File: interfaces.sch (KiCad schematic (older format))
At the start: 55 parts, among them J6 0878311420, J7 61300611121, U14 XC7A100T-FGG484, U17 EMMC04G-S100-B08U, U18 MAX3421EEHJ, U19 FT245RQ, U6 NVT2008DQ,115, Y1 ABM8G-12.000MHZ-18-D2Y-T

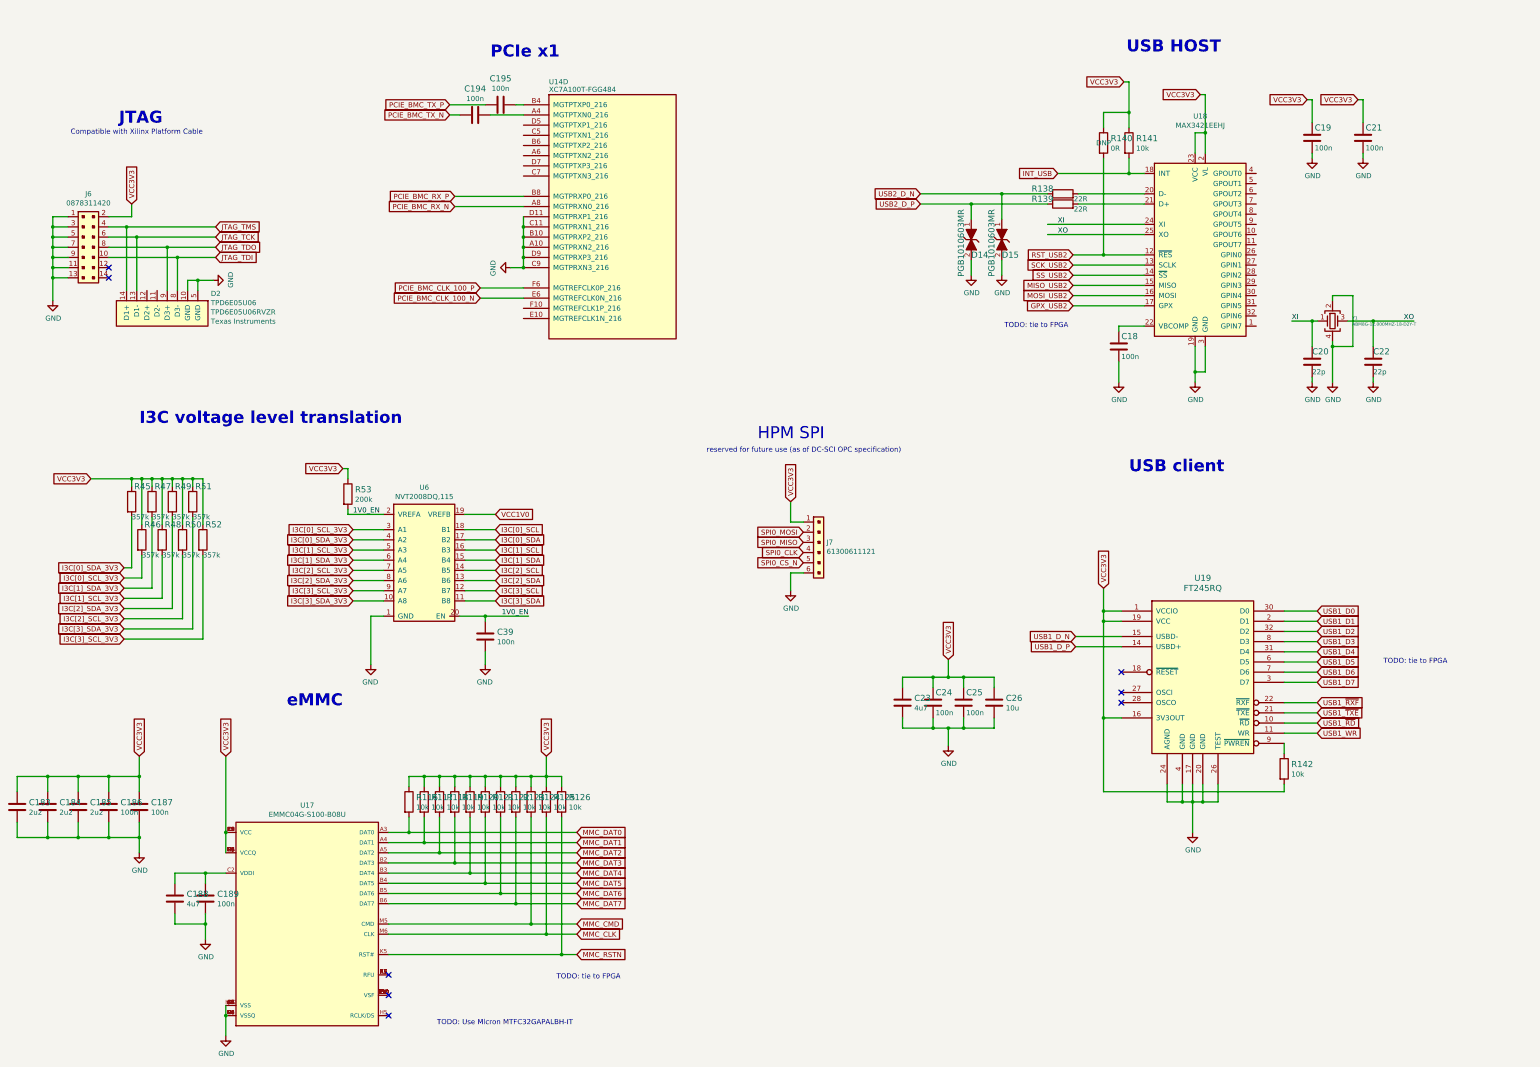
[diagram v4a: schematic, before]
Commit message: Added USB3300 controllers
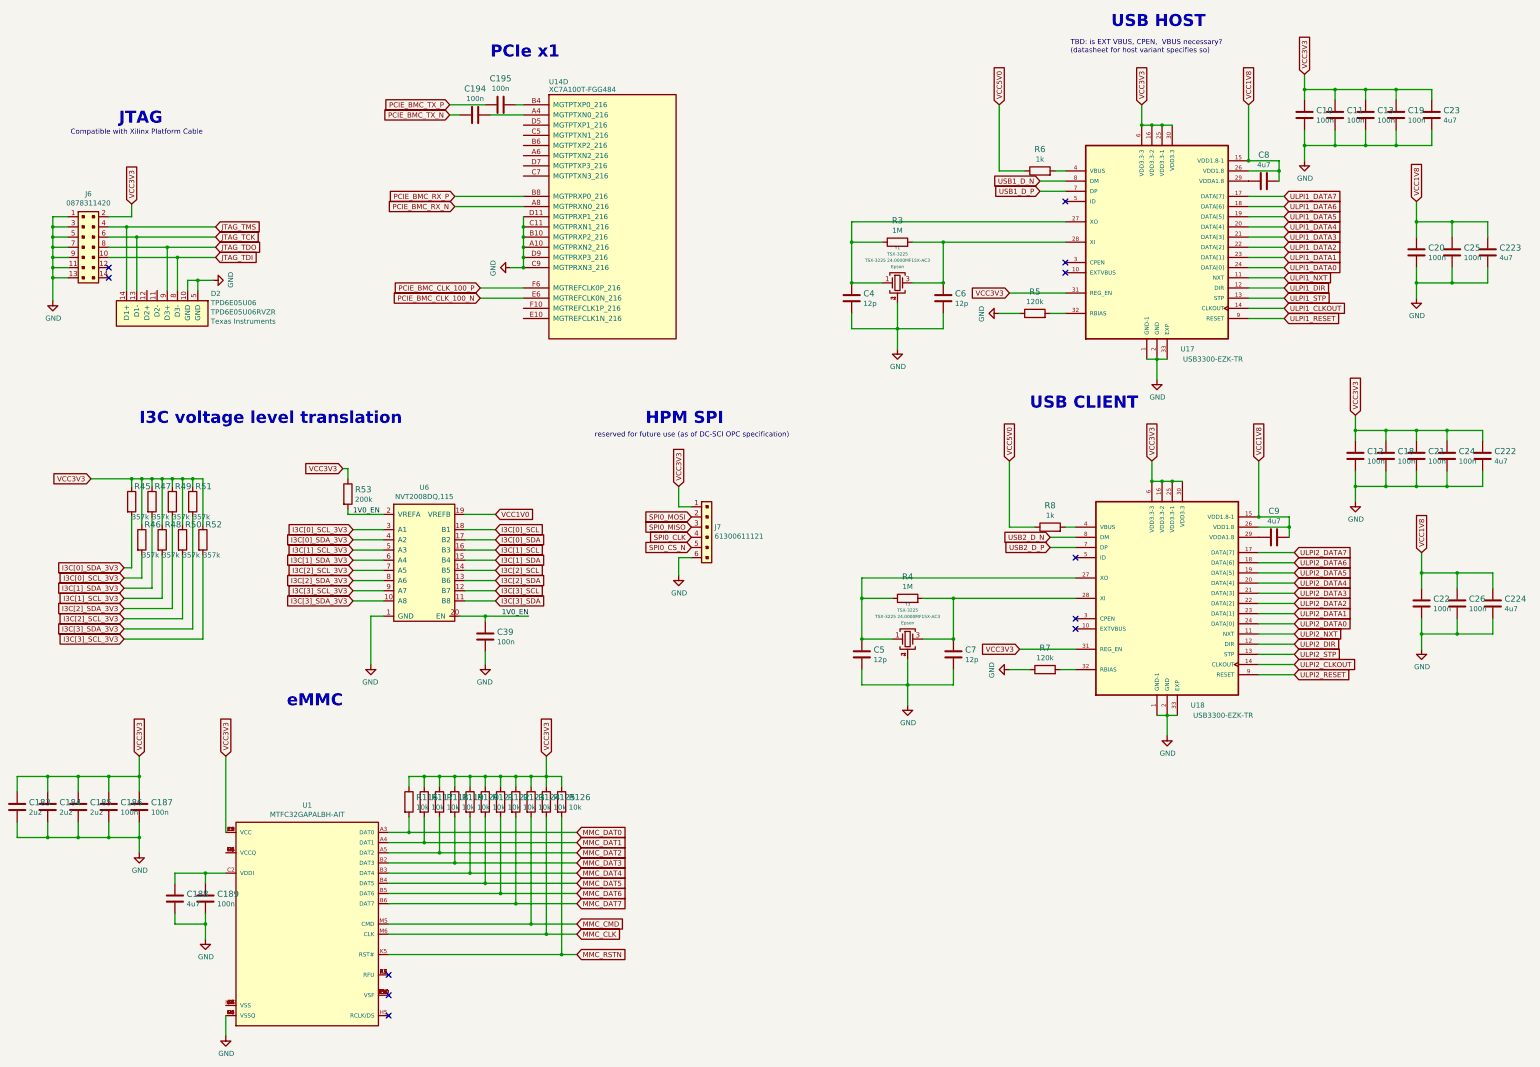
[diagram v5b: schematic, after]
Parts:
- removed C18, C19, C21, C24, C25: C_100n_0402, artix-dc-scm-footprints:0402-cap, symbol artix-dc-scm:C_100n_0402-artix-dc-scm
- removed C20, C22: C_22p_0402, artix-dc-scm-footprints:0402-cap, symbol artix-dc-scm:C_22p_0402
- removed C23: C_4u7_0402, artix-dc-scm-footprints:0402-cap, symbol artix-dc-scm:C_4u7_0402
- removed C26: C_10u_0402, artix-dc-scm-footprints:0402-cap, symbol artix-dc-scm:C_10u_0402
- removed D14, D15: PGB1010603MR, artix-dc-scm-footprints:PGB1010603MR, symbol artix-dc-scm:PGB1010603MR
- removed R138, R139: R_22R_0402, artix-dc-scm-footprints:0402-res, symbol artix-dc-scm:R_22R_0402
- removed R140: R_0R_0402, artix-dc-scm-footprints:0402-res, symbol artix-dc-scm:R_0R_0402
- removed R141, R142: R_10k_0402, artix-dc-scm-footprints:0402-res, symbol artix-dc-scm:R_10k_0402
- removed U17: EMMC04G-S100-B08U, artix-dc-scm-footprints:MICRON_EMMC_153, symbol artix-dc-scm:EMMC04G-S100-B08U
- removed U18: MAX3421EEHJ, artix-dc-scm-footprints:TQFP-32_5x5mm, symbol artix-dc-scm:MAX3421EEHJ
- removed U19: FT245RQ, artix-dc-scm-footprints:QFN-32-1EP_5x5mm, symbol artix-dc-scm:FT245RQ
- removed Y1: ABM8G-12.000MHZ-18-D2Y-T, artix-dc-scm-footprints:KX-7, symbol artix-dc-scm:ABM8G-12.000MHZ-18-D2Y-T
- added C10, C11, C12, C13, C18, C19, C20, C21, C22, C24, C25, C26: C_100n_0402, antmicro-footprints:0402-cap, symbol antmicroCapacitors0402:C_100n_0402
- added C222, C223, C224, C23, C8, C9: C_4u7_0402, antmicro-footprints:0402-cap, symbol antmicroCapacitors0402:C_4u7_0402
- added C4, C5, C6, C7: C_12p_0402, antmicro-footprints:0402-cap, symbol antmicroCapacitors0402:C_12p_0402
- added R3, R4: R_1M_0603, antmicro-footprints:0603-res, symbol antmicroResistors0603:R_1M_0603
- added R5, R7: R_120k_0402, antmicro-footprints:0402-res, symbol antmicroResistors0402:R_120k_0402
- added R6, R8: R_1k_0402, antmicro-footprints:0402-res, symbol antmicroResistors0402:R_1k_0402
- added U1: MTFC32GAPALBH-AIT, antmicro-footprints:MICRON_EMMC_153, symbol antmicroMemory:MTFC32GAPALBH-AIT
- added U17, U18: USB3300-EZK-TR, QFN50P500X500X100-33N, symbol antmicroInterfaceControllers:USB3300-EZK-TR
- added Y1, Y3: TSX-3225, antmicro-footprints:KX-7, symbol antmicroCrystals:TSX-3225
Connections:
- net GND: now also C10.2, C11.2, C12.2, C13.2, C18.2, C19.2, C20.2, C21.2, C22.2, C222.2, C223.2, C224.2, C23.2, C24.2, C25.2, C26.2, C4.2, C5.2, C6.2, C7.2, R5.1, R7.1, U1.C4 (VSSQ), U1.N2 (VSSQ), U1.N5 (VSSQ), U1.P4 (VSSQ), U1.P6 (VSSQ), U17.1 (GND-1), U17.2 (GND), U17.33 (EXP), U18.1 (GND-1), U18.2 (GND), U18.33 (EXP), Y1.2, Y1.4, Y3.2, Y3.4
- net MMC_CLK: now also U1.M6 (CLK)
- net MMC_CMD: now also U1.M5 (CMD)
- net MMC_DAT0: now also U1.A3 (DAT0)
- net MMC_DAT1: now also U1.A4 (DAT1)
- net MMC_DAT2: now also U1.A5 (DAT2)
- net MMC_DAT3: now also U1.B2 (DAT3)
- net MMC_DAT4: now also U1.B3 (DAT4)
- net MMC_DAT5: now also U1.B4 (DAT5)
- net MMC_DAT6: now also U1.B5 (DAT6)
- net MMC_DAT7: now also U1.B6 (DAT7)
- net MMC_RSTN: now also U1.K5 (RST#)
- net USB1_D_N: now also U17.8 (DM)
- net USB1_D_P: now also U17.7 (DP)
- net USB2_D_N: now also U18.8 (DM)
- net USB2_D_P: now also U18.7 (DP)
- net VCC3V3: now also C10.1, C11.1, C12.1, C13.1, C18.1, C19.1, C21.1, C222.1, C23.1, C24.1, U1.E6 (VCC), U1.F5 (VCC), U1.J10 (VCC), U1.K9 (VCC), U17.16 (VDD3.3-2), U17.25 (VDD3.3-1), U17.30 (VDD3.3), U17.31 (REG_EN), U17.6 (VDD3.3-3), U18.16 (VDD3.3-2), U18.25 (VDD3.3-1), U18.30 (VDD3.3), U18.31 (REG_EN), U18.6 (VDD3.3-3)
- net at C188.1, C189.1: now also U1.C2 (VDDI)
- new net: C4.1, R3.1, U17.27 (XO), Y1.1
- new net: C6.1, R3.2, U17.28 (XI), Y1.3
- new net: C8.2, U17.29 (VDDA1.8)
- new net: R5.2, U17.32 (RBIAS)
- new net: R6.2, U17.4 (VBUS)
- new net: C5.1, R4.1, U18.27 (XO), Y3.1
- new net: C7.1, R4.2, U18.28 (XI), Y3.3
- new net: C9.2, U18.29 (VDDA1.8)
- new net: R7.2, U18.32 (RBIAS)
- new net: R8.2, U18.4 (VBUS)
- new net: U1.A6 (VSS), U1.E7 (VSS), U1.G5 (VSS), U1.H10 (VSS), U1.J5 (VSS), U1.K8 (VSS)
- new net: U1.A7 (RFU), U1.E5 (RFU), U1.K6 (RFU), U1.K7 (RFU)
- new net: U1.C6 (VCCQ), U1.M4 (VCCQ), U1.N4 (VCCQ), U1.P3 (VCCQ), U1.P5 (VCCQ)
- new net: U1.E10 (VSF), U1.E8 (VSF), U1.E9 (VSF), U1.F10 (VSF), U1.G10 (VSF), U1.K10 (VSF), U1.P10 (VSF)
- new net ULPI1_CLKOUT: U17.14 (CLKOUT)
- new net ULPI1_DATA0: U17.24 (DATA[0])
- new net ULPI1_DATA1: U17.23 (DATA[1])
- new net ULPI1_DATA2: U17.22 (DATA[2])
- new net ULPI1_DATA3: U17.21 (DATA[3])
- new net ULPI1_DATA4: U17.20 (DATA[4])
- new net ULPI1_DATA5: U17.19 (DATA[5])
- new net ULPI1_DATA6: U17.18 (DATA[6])
- new net ULPI1_DATA7: U17.17 (DATA[7])
- new net ULPI1_DIR: U17.12 (DIR)
- new net ULPI1_NXT: U17.11 (NXT)
- new net ULPI1_RESET: U17.9 (RESET)
- new net ULPI1_STP: U17.13 (STP)
- new net ULPI2_CLKOUT: U18.14 (CLKOUT)
- new net ULPI2_DATA0: U18.24 (DATA[0])
- new net ULPI2_DATA1: U18.23 (DATA[1])
- new net ULPI2_DATA2: U18.22 (DATA[2])
- new net ULPI2_DATA3: U18.21 (DATA[3])
- new net ULPI2_DATA4: U18.20 (DATA[4])
- new net ULPI2_DATA5: U18.19 (DATA[5])
- new net ULPI2_DATA6: U18.18 (DATA[6])
- new net ULPI2_DATA7: U18.17 (DATA[7])
- new net ULPI2_DIR: U18.12 (DIR)
- new net ULPI2_NXT: U18.11 (NXT)
- new net ULPI2_RESET: U18.9 (RESET)
- new net ULPI2_STP: U18.13 (STP)
- new net VCC1V8: C20.1, C22.1, C223.1, C224.1, C25.1, C26.1, C8.1, C9.1, U17.15 (VDD1.8-1), U17.26 (VDD1.8), U18.15 (VDD1.8-1), U18.26 (VDD1.8)
- new net VCC5V0: R6.1, R8.1
- no-connect marks 8 -> 11
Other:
- note added: "TBD: is EXT VBUS, CPEN, VBUS necessary?\n(datasheet for host variant specifies so)"
- note added: "USB CLIENT"
- note removed: "TODO: Use Micron MTFC32GAPALBH-IT"
- note removed: "TODO: tie to FPGA"
- note removed: "USB client"
- moved on the sheet: J7

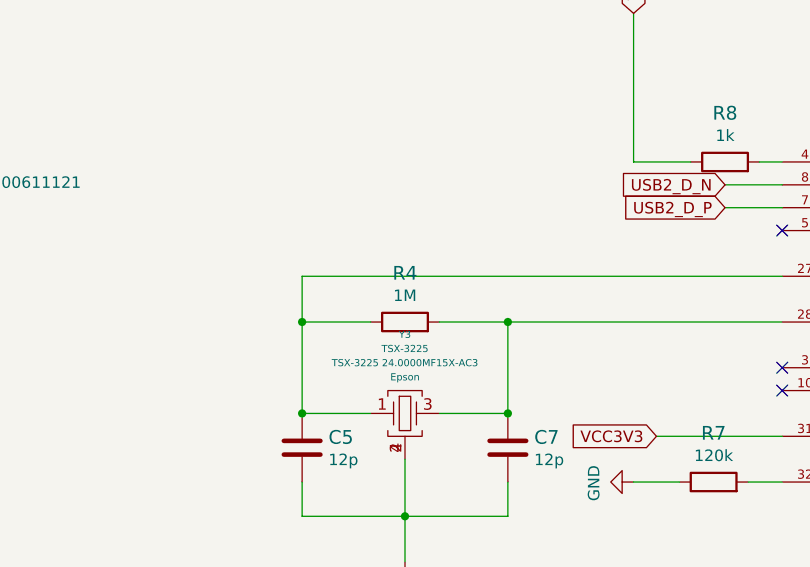
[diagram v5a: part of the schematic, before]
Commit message: Add layout for ULPI USB2
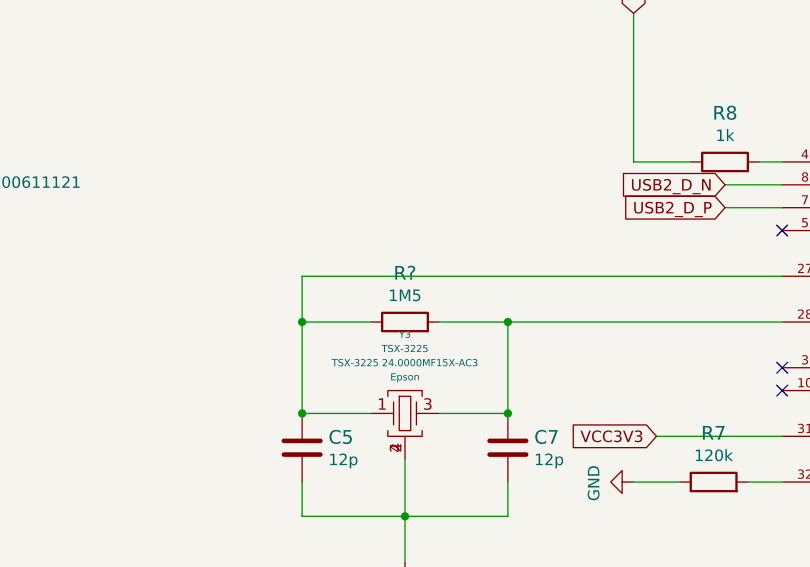
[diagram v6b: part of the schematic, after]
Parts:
- removed R4: R_1M_0603, antmicro-footprints:0603-res, symbol antmicroResistors0603:R_1M_0603
- added R?: R_1M5_0402, antmicro-footprints:0402-res, symbol antmicroResistors0402:R_1M5_0402
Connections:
- net at C5.1, U18.27 (XO), Y3.1: now also R?.1
- net at C7.1, U18.28 (XI), Y3.3: now also R?.2
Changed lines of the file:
@@
-$EndComp
-$Comp
-L antmicroResistors0603:R_1M_0603 R4
-U 1 1 601F5896
-P 9750 6600
-F 0 "R4" H 9750 6813 60  0000 C CNN
-F 1 "R_1M_0603" H 9750 6450 60  0001 C CNN
-F 2 "antmicro-footprints:0603-res" H 9950 6800 60  0001 L CNN
-F 3 "" H 9750 6600 50  0001 C CNN
-F 4 "BOURNS" H 9950 7000 60  0001 L CNN "Manufacturer"
-F 5 "CR0603-JW-105GLF" H 9950 6900 60  0001 L CNN "MPN"
-F 6 "1M" H 9750 6715 50  0000 C CNN "Val"
-	1    9750 6600
-	1    0    0    -1
 $EndComp
 $Comp
@@
 Text Notes 11350 1250 0    50   ~ 0
 TBD: is EXT VBUS, CPEN,  VBUS necessary?\n(datasheet for host variant specifies so)
+$Comp
+L antmicroResistors0402:R_1M5_0402 R?
+U 1 1 603E998C
+P 9750 6600
+F 0 "R?" H 9750 6813 60  0000 C CNN
+F 1 "R_1M5_0402" H 9750 6450 60  0001 C CNN
+F 2 "antmicro-footprints:0402-res" H 9950 6800 60  0001 L CNN
+F 3 "" H 9750 6600 50  0001 C CNN
+F 4 "MULTICOMP" H 9950 7000 60  0001 L CNN "Manufacturer"
+F 5 "MCWR04W1504FTL" H 9950 6900 60  0001 L CNN "MPN"
+F 6 "1M5" H 9750 6715 50  0000 C CNN "Val"
+	1    9750 6600
+	1    0    0    -1
+$EndComp
 $EndSCHEMATC
